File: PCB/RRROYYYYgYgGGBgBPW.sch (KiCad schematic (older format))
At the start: 36 parts, among them K1 CONN_6, SW1 SPST, SW2 SW_PUSH, SW3 SW_PUSH, U1 ATTINY85-M, U2 AAT1217-3.3, U3 74HC595, U4 74HC595

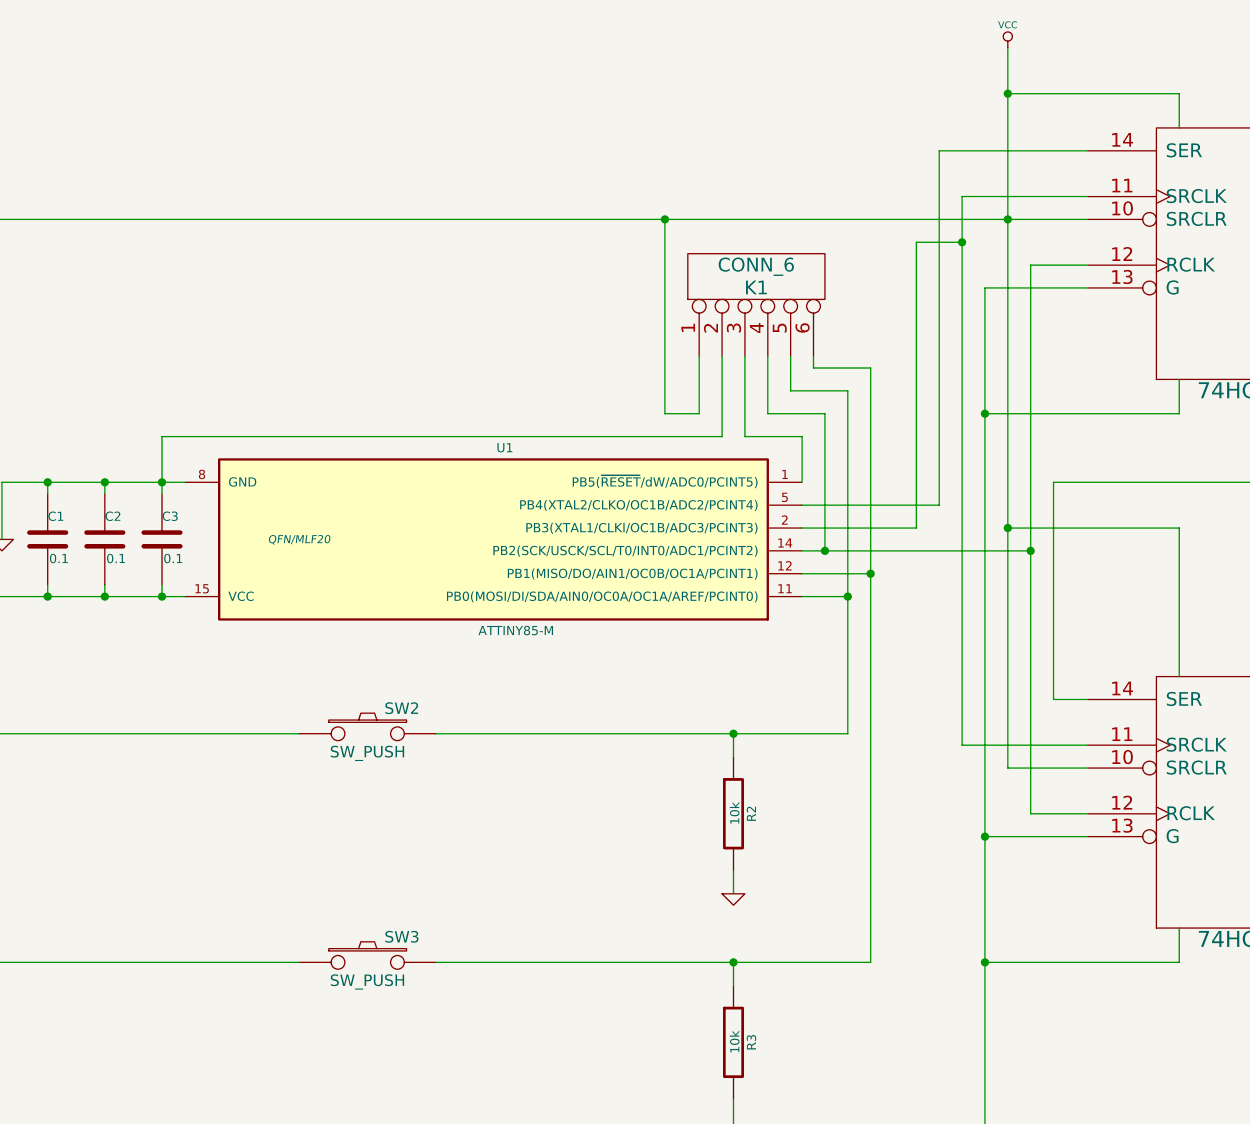
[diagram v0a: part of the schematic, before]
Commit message: changed the file names to reflect addition of pink and white LEDs. finished routing, beefed up power rails, rounded corners. changed processor footprint to TSSOP. still needs a thorough review...
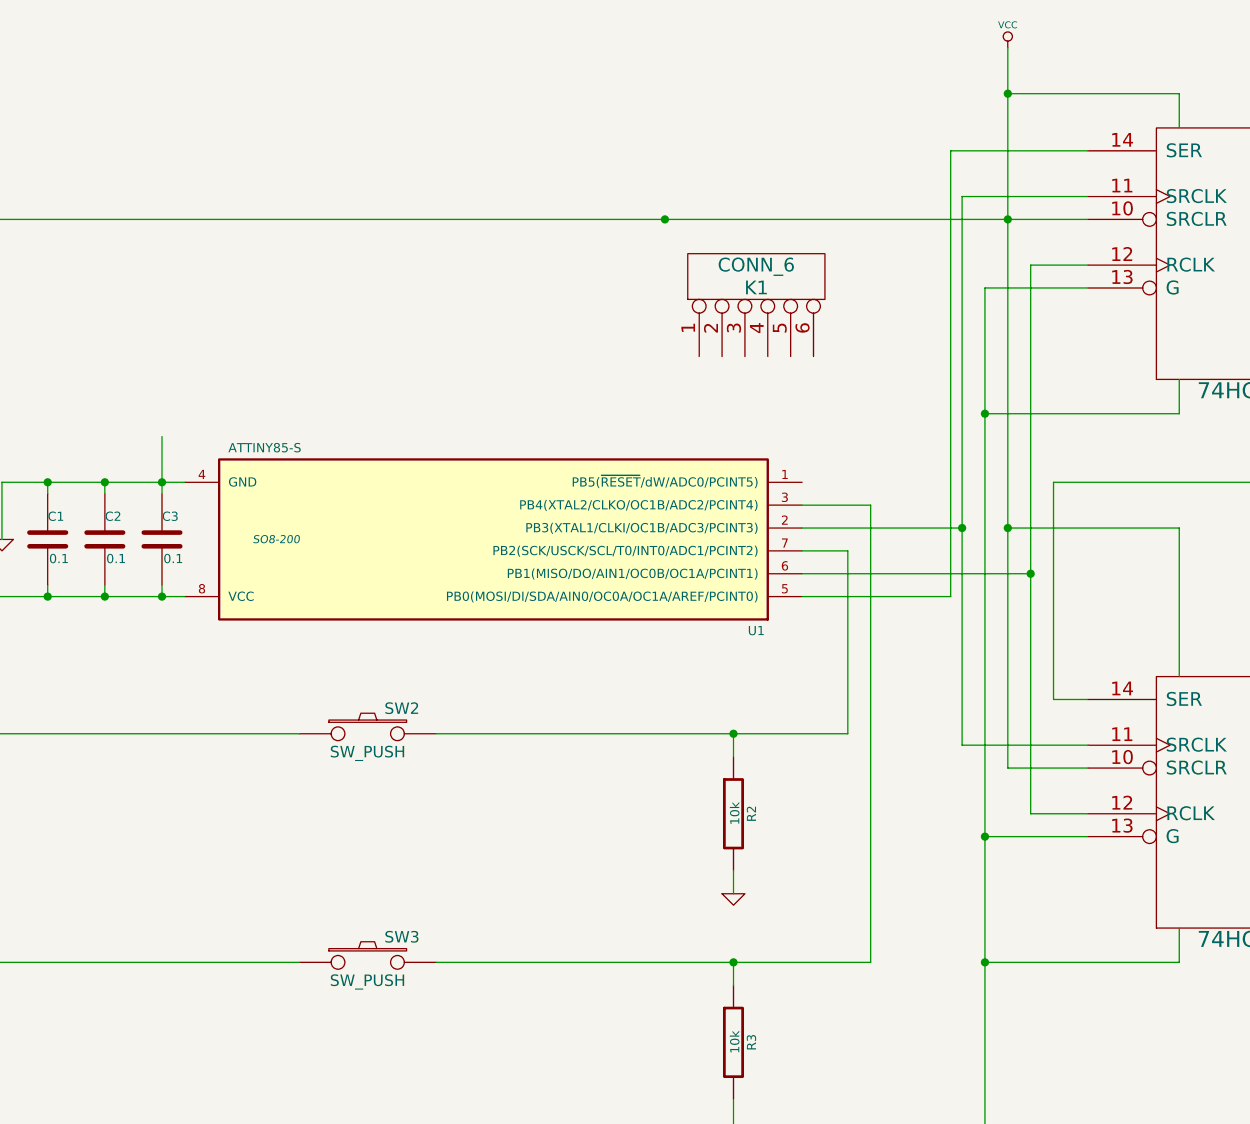
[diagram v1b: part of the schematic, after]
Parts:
- removed U1: ATTINY85-M, QFN/MLF20, symbol ATTINY85-M
- added U1: ATTINY85-S, SO8-200, symbol ATTINY85-S
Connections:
- net GND: now also U1.4 (GND); no longer K1.2
- net VCC: now also U1.8 (VCC); no longer K1.1
- net at U3.11 (SRCLK), U4.11 (SRCLK): now also U1.2 (PB3(XTAL1/CLKI/OC1B/ADC3/PCINT3))
- net at U3.12 (RCLK), U4.12 (RCLK): now also U1.6 (PB1(MISO/DO/AIN1/OC0B/OC1A/PCINT1)); no longer K1.4
- net at U3.14 (SER): now also U1.5 (PB0(MOSI/DI/SDA/AIN0/OC0A/OC1A/AREF/PCINT0))
- net at R2.1, SW2.2: now also U1.7 (PB2(SCK/USCK/SCL/T0/INT0/ADC1/PCINT2)); no longer K1.5
- net at R3.1, SW3.2: now also U1.3 (PB4(XTAL2/CLKO/OC1B/ADC2/PCINT4)); no longer K1.6
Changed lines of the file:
@@
 Sheet 1 1
 Title ""
-Date "8 nov 2015"
+Date "10 nov 2015"
 Rev ""
 Comp ""
@@
 	1    5800 5850
 	1    0    0    -1
-$EndComp
-$Comp
-L ATTINY85-M U1
-U 1 1 563AC0C3
-P 3650 2950
-F 0 "U1" H 3600 2550 40  0000 C CNN
-F 1 "ATTINY85-M" H 3550 3350 40  0000 C CNN
-F 2 "QFN/MLF20" H 4500 2950 35  0000 C CIN
-F 3 "" H 3650 2950 60  0000 C CNN
-	1    3650 2950
-	-1   0    0    1
 $EndComp
 $Comp
@@
 	1    0    0    -1
 $EndComp
+$Comp
+L ATTINY85-S U1
+U 1 1 564253CE
+P 3650 2950
+F 0 "U1" H 2500 3350 40  0000 C CNN
+F 1 "ATTINY85-S" H 4650 2550 40  0000 C CNN
+F 2 "SO8-200" H 4600 2950 35  0000 C CIN
+F 3 "" H 3650 2950 60  0000 C CNN
+	1    3650 2950
+	-1   0    0    1
+$EndComp
 Wire Wire Line
 	9600 3650 9550 3650
@@
 Wire Wire Line
 	3000 5750 3000 6500
-Connection ~ 5300 3100
-Wire Wire Line
-	5050 2200 5300 2200
-Wire Wire Line
-	5050 2150 5050 2200
-Connection ~ 5200 3200
-Wire Wire Line
-	4950 2300 5200 2300
-Wire Wire Line
-	4950 2150 4950 2300
-Connection ~ 5100 3000
-Wire Wire Line
-	5100 2400 5100 3000
-Wire Wire Line
-	4850 2400 5100 2400
-Wire Wire Line
-	4850 2150 4850 2400
 Connection ~ 4400 1550
-Wire Wire Line
-	4400 2400 4400 1550
-Wire Wire Line
-	4550 2400 4400 2400
-Wire Wire Line
-	4550 2150 4550 2400
-Wire Wire Line
-	4650 2500 4650 2150
-Wire Wire Line
-	2200 2500 4650 2500
-Wire Wire Line
-	4750 2500 4750 2150
-Wire Wire Line
-	5000 2500 4750 2500
-Wire Wire Line
-	5000 2700 5000 2500
 Connection ~ 5800 4800
 Wire Wire Line
@@
 Connection ~ 1300 3800
 Connection ~ 1300 3200
-Wire Wire Line
-	5200 2300 5200 3800
-Wire Wire Line
-	5300 2200 5300 4800
-Wire Wire Line
-	5000 3100 5300 3100
-Wire Wire Line
-	5200 3200 5000 3200
 Connection ~ 1700 2700
 Wire Wire Line
@@
 	1300 3200 2300 3200
 Wire Wire Line
-	5000 3000 6000 3000
-Wire Wire Line
-	5500 2900 5000 2900
-Wire Wire Line
-	5000 2800 5600 2800
-Connection ~ 6000 3000
-Connection ~ 5700 1650
-Wire Wire Line
-	5500 1650 5700 1650
-Wire Wire Line
-	5500 2900 5500 1650
-Wire Wire Line
-	5600 1250 6250 1250
-Wire Wire Line
-	5600 2800 5600 1250
-Wire Wire Line
 	1300 1550 1300 4800
 Wire Wire Line
 	5700 1450 6250 1450
-Wire Wire Line
-	5700 1450 5700 3850
 Wire Wire Line
 	5700 3850 6250 3850
@@
 Wire Wire Line
 	8850 3650 9150 3650
+Wire Wire Line
+	5000 3000 5200 3000
+Wire Wire Line
+	5200 3000 5200 3800
+Wire Wire Line
+	5300 2800 5300 4800
+Wire Wire Line
+	5300 2800 5000 2800
+Wire Wire Line
+	5000 2900 5700 2900
+Connection ~ 5700 2900
+Wire Wire Line
+	5000 3200 5650 3200
+Wire Wire Line
+	5650 3200 5650 1250
+Wire Wire Line
+	5650 1250 6250 1250
+Wire Wire Line
+	5700 1450 5700 3850
+Wire Wire Line
+	5000 3100 6000 3100
+Connection ~ 6000 3100
 $EndSCHEMATC

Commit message: changed from 3.3vdc boost converter + 2032 coin cell to usb plug power. added silkscreen, re-routed, etc. resistor network value still TBD, i'm afraid (it worked at 3.3vdc, but might not here...)
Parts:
- removed BT1: BATTERY, ~, symbol BATTERY
- removed C4, C5: 4.7 uF, ~, symbol C
- removed K1: CONN_6, symbol CONN_6
- removed L1: 4.7 uH, ~, symbol INDUCTOR
- removed R1: 1M, ~, symbol R
- removed SW1: SPST, ~, symbol SPST
- removed U2: AAT1217-3.3, symbol AAT1217-3.3
- added CONN1: USB_PLUG, ~, symbol USB_PLUG
- added P1: VCC, symbol CONN_1
- added P2: GND, symbol CONN_1
- added P3: RST, symbol CONN_1
- added P4: SCK, symbol CONN_1
- added P5: MISO, symbol CONN_1
- added P6: MOSI, symbol CONN_1
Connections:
- net GND: now also CONN1.4 (GND), P2.1
- net VCC: now also CONN1.1 (VCC), P1.1
- net at U1.6 (PB1(MISO/DO/AIN1/OC0B/OC1A/PCINT1)), U3.12 (RCLK), U4.12 (RCLK): now also P5.1
- net at U1.5 (PB0(MOSI/DI/SDA/AIN0/OC0A/OC1A/AREF/PCINT0)), U3.14 (SER): now also P6.1
- net at R2.1, SW2.2, U1.7 (PB2(SCK/USCK/SCL/T0/INT0/ADC1/PCINT2)): now also P4.1
- net at U1.1 (PB5(~RESET~/dW/ADC0/PCINT5)): now also P3.1

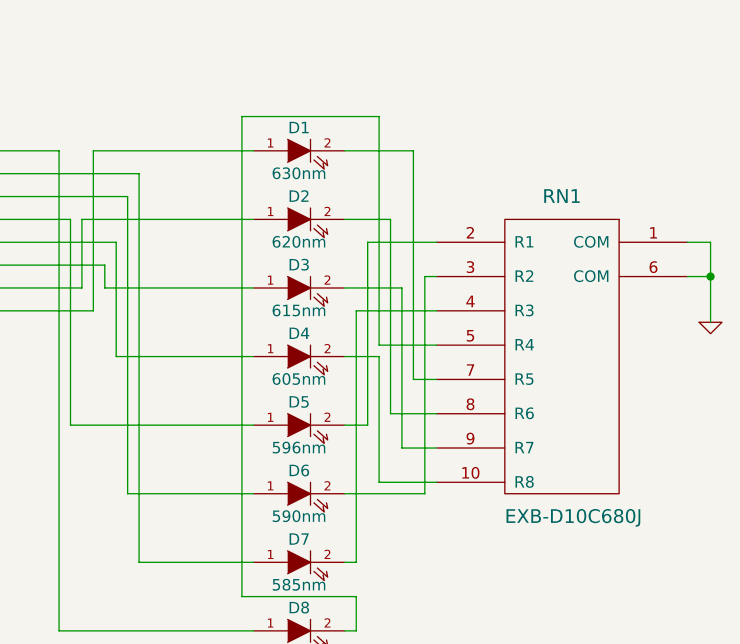
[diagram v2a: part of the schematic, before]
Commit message: realized the resistor networks were sized for 3.3vdc power; moving to 5vdc power means the shorter wavelength stuff needs a different value. bodged in a quartet of 0402 resistors, mounted on the back. symmetry is pretty much horrible now.
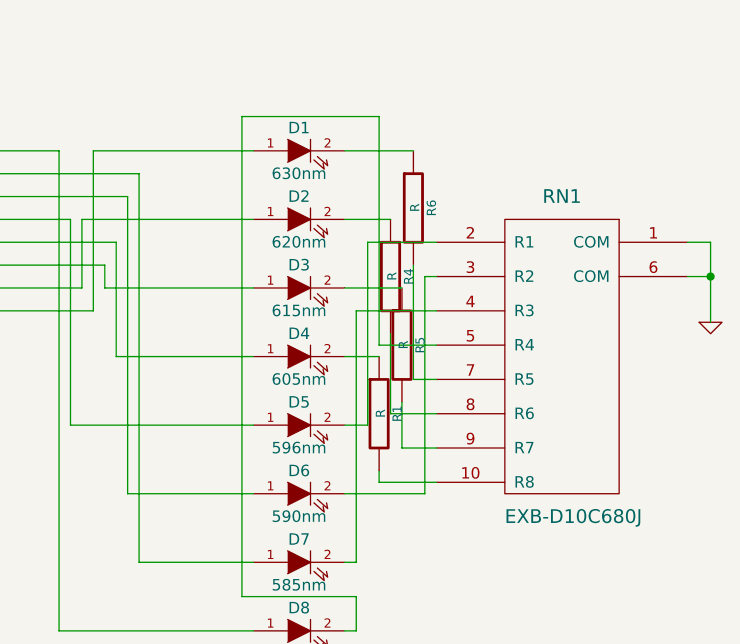
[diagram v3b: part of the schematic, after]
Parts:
- added R1, R4, R5, R6: R, ~, symbol R
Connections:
- net at D1.2 (K): now also R6.1; no longer RN1.7 (R5)
- net at D2.2 (K): now also R4.1; no longer RN1.8 (R6)
- net at D3.2 (K): now also R5.1; no longer RN1.9 (R7)
- net at D4.2 (K): now also R1.1; no longer RN1.10 (R8)
- new net: R1.2, RN1.10 (R8)
- new net: R6.2, RN1.7 (R5)
- new net: R4.2, RN1.8 (R6)
- new net: R5.2, RN1.9 (R7)
